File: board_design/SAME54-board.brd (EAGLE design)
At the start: 86.2 x 72.6 mm, 28 parts, among them IC1 ATSAME54N20A-AUT, J2 1985920

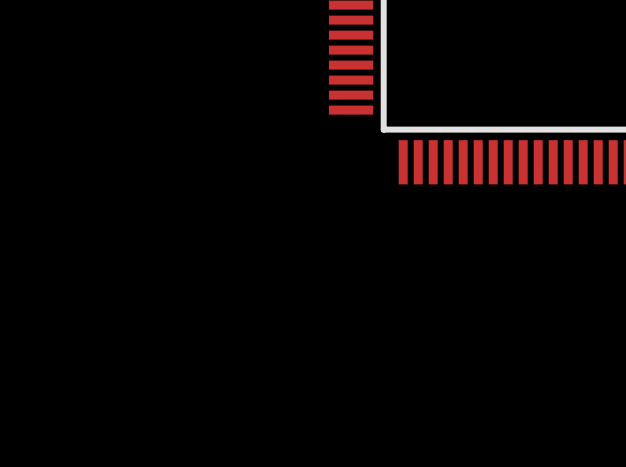
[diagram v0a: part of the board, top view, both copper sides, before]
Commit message: Added power and max20034 to schematic
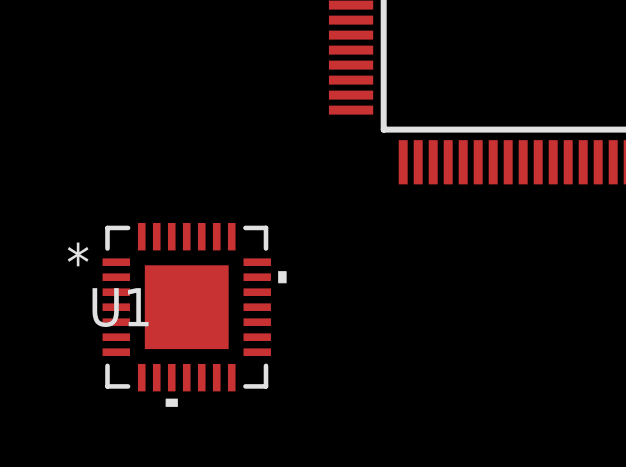
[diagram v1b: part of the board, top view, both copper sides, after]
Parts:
- added U1: MAX20034ATIS/VY+, LAMS_lib:21-100130_MXM
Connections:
- new net AGND: U1.9
- new net EPAD: U1.29
- new net PGND1: U1.3
- new net PGND2: U1.20
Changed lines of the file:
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@@
 <attribute name="VALUE" x="-33.02" y="35.81" size="1.27" layer="27" align="center"/>
+</element>
+<element name="U1" library="LAMS_lib" package="21-100130_MXM" value="MAX20034ATIS/VY+" x="-69.095034375" y="-3.679315625" smashed="yes">
+<attribute name="MANUFACTURER_PART_NUMBER" value="MAX20034ATISVY+" x="-69.095034375" y="-3.679315625" size="1.778" layer="27" display="off"/>
+<attribute name="NAME" x="-72.371634375" y="-4.314315625" size="1.27" layer="25" ratio="6" rot="SR0"/>
+<attribute name="VENDOR" value="Maxim Integrated Products" x="-69.095034375" y="-3.679315625" size="1.778" layer="27" display="off"/>
 </element>
 </elements>
@@
 <contactref element="IC1" pad="26"/>
 </signal>
+<signal name="PGND1">
+<contactref element="U1" pad="3"/>
+</signal>
+<signal name="AGND">
+<contactref element="U1" pad="9"/>
+</signal>
+<signal name="PGND2">
+<contactref element="U1" pad="20"/>
+</signal>
+<signal name="EPAD">
+<contactref element="U1" pad="29"/>
+</signal>
 </signals>

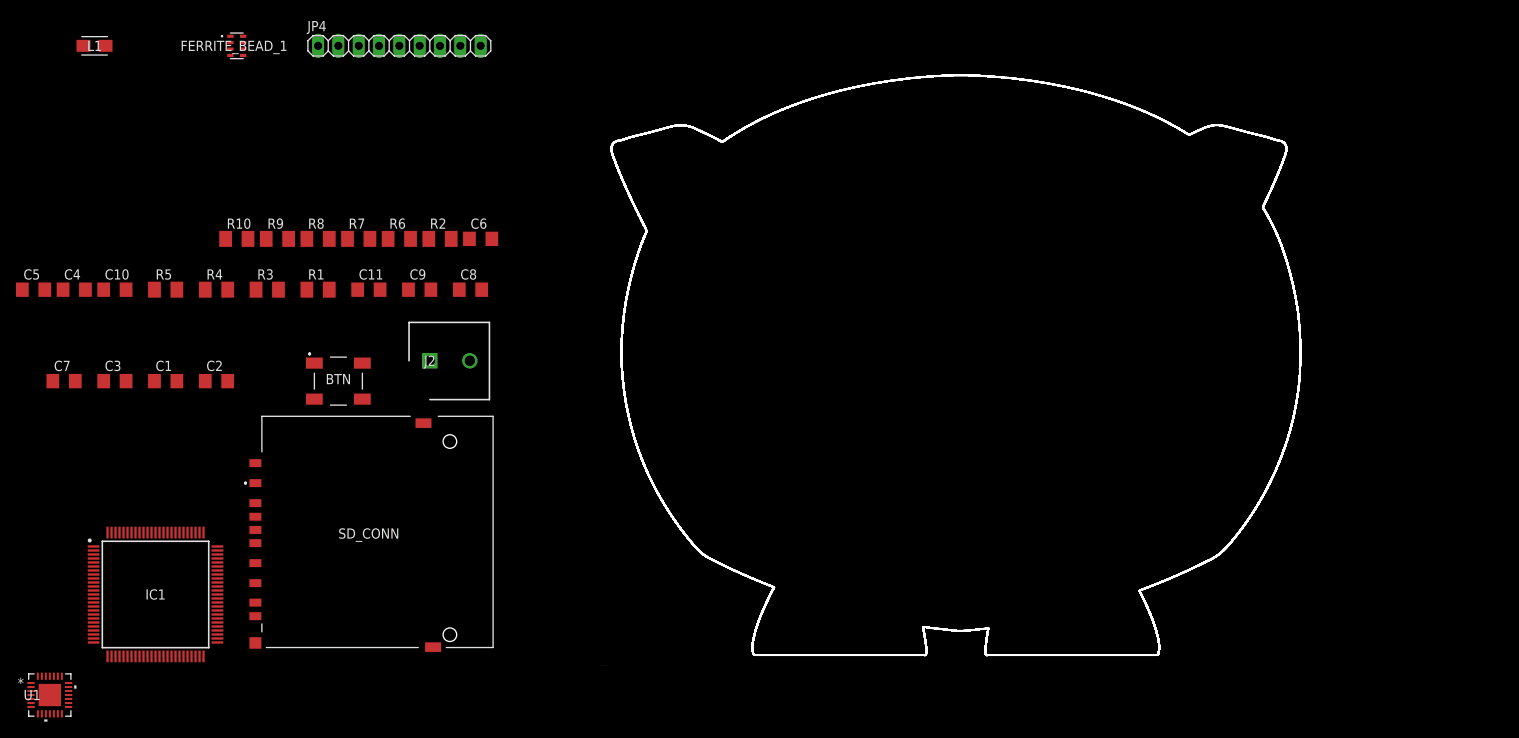
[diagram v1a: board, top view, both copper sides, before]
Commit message: Finished custom SAME54 design. Ready to order
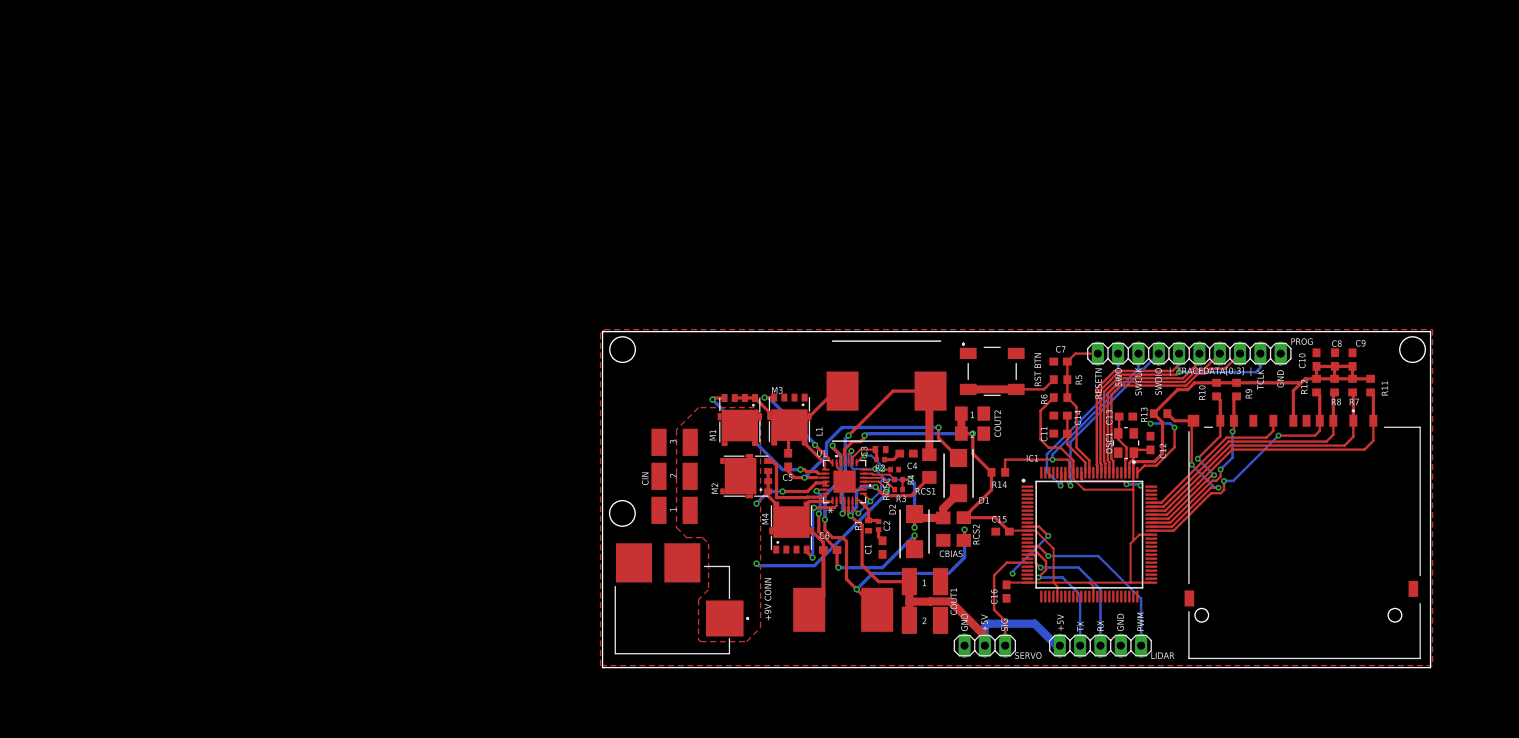
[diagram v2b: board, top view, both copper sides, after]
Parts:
- removed BTN: LL3301BF065QJ, SamacSys_Parts:LL3301BF065QJ
- removed FERRITE_BEAD_1: BLA31AG221SN4D, SamacSys_Parts:BLA31AG102SN4D
- removed J2: 1985920, SamacSys_Parts:SHDR2W110P0X500_1X2_1000X950X1
- removed JP4: (no value), pinhead:1X09
- removed SD_CONN: GSD09002SEU, SamacSys_Parts:GSD09002SEU
- added C12, C13: 8p, rcl:C0603
- added C14: 4.7u, rcl:C0603
- added C15, C16: 100n, rcl:C0603
- added CBIAS: 6.8u, rcl:C1206
- added CIN_1, CIN_2, CIN_3, COUT1_1, COUT1_2: 33u, rcl:C1812
- added COUT2_1, COUT2_2: 22u, rcl:C1206
- added D1, D2: MBRS140T3G, LAMS_lib:DIOM5436X247N
- added J1: PJ-070BH-SMT-TR, LAMS_lib:PJ070BHSMTTR
- added L2: MSS1260-682MLB, LAMS_lib:MSS1260
- added LIDAR: (no value), pinhead:1X05
- added M1, M2, M3, M4: NVMFS5C468NL, LAMS_lib:DFN5_SO-8FL
- added OSC1: CX3225CA12000D0KPSC1CX3225CA, LAMS_lib:OSCCC320X250X90N
- added PROG: (no value), pinhead:1X10
- added R11: 100k, rcl:R0603
- added R12, R13: 10k, rcl:R0603
- added R14: 1k, rcl:R0603
- added RCS1: 8.2m, rcl:R1206
- added RCS2: 20m, rcl:R1206
- added RESET_BTN: LL3301BF065QJ, LAMS_lib:LL3301BF065QJ
- added ROSC: 46.4k, rcl:R0402
- added SD_CARD_CONN: GSD09002SEU, LAMS_lib:GSD09002SEU
- added SERVO: (no value), pinhead:1X03
- C1: value 100n -> 4.7n; device rcl:C1206 -> rcl:C0603
- C10: value 4.7u -> 100n; device rcl:C1206 -> rcl:C0603
- C11, C7, C8: device rcl:C1206 -> rcl:C0603
- C2: value 10uF/10V -> 4.7p; device rcl:C1206 -> rcl:C0402
- C3: value 100n -> 4.7p; device rcl:C1206 -> rcl:C0402
- C4: value 10u -> 4.7n; device rcl:C1206 -> rcl:C0603
- C5, C6: value 10u -> 100n; device rcl:C1206 -> rcl:C0603
- C9: value 100n -> 10u; device rcl:C1206 -> rcl:C0603
- IC1: device SamacSys_Parts:QFP50P1600X1600X120-100N -> LAMS_lib:QFP50P1600X1600X120-100N
- L1: value LQH31MN100J03L -> SRP1238A-3R3M; device SamacSys_Parts:LQH31CN100K03L -> LAMS_lib:INDPM135125X350N
- R1: value 100k -> 10.5k; device rcl:M1206 -> rcl:R0402
- R10: value 1k -> 100k; device rcl:M1206 -> rcl:R0603
- R2: value 10k -> 10.2k; device rcl:M1206 -> rcl:R0402
- R3, R4: value 100k -> 51k; device rcl:M1206 -> rcl:R0402
- R5: value 100k -> 330; device rcl:M1206 -> rcl:R0603
- R6, R8: device rcl:M1206 -> rcl:R0603
- R7: value 10k -> 100k; device rcl:M1206 -> rcl:R0603
- R9: value 330 -> 100k; device rcl:M1206 -> rcl:R0603
- moved C10 150.5 mm to (89.2, 38.2), turned to 90 degrees
- moved R8 128.4 mm to (91.5, 35.0), turned to 90 degrees
- moved R7 125.6 mm to (93.8, 35.0), turned to 90 degrees
- moved C7 124.6 mm to (57.2, 38.0), turned to 180 degrees
- moved R10 123.9 mm to (76.8, 34.5), turned to 90 degrees
- moved R9 121.4 mm to (79.2, 34.5), turned to 90 degrees
- moved IC1 117.0 mm to (60.9, 16.4)
- moved C9 116.9 mm to (93.8, 38.2), turned to 90 degrees
- moved R5 112.4 mm to (57.2, 35.8)
- moved C8 108.4 mm to (91.5, 38.3), turned to 90 degrees
- moved L1 108.0 mm to (35.5, 34.3)
- moved C4 106.0 mm to (38.0, 26.5)
- moved U1 102.9 mm to (30.2, 23.0), turned to 90 degrees
- moved C5 96.7 mm to (23.2, 25.7), turned to 270 degrees
- moved C3 96.1 mm to (34.8, 27.0)
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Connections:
- removed net AGND: U1.9
- removed net EPAD: U1.29
- removed net N$2: R2.1, SD_CONN.2
- removed net PGND1: U1.3
- removed net PGND2: U1.20
- removed net SDDAT[0]: IC1.27, R3.1, SD_CONN.7
- removed net SDDAT[1]: IC1.28, R4.1, SD_CONN.8
- removed net SDDAT[2]: IC1.29, R5.1, SD_CONN.9
- removed net SDDAT[3]: IC1.32, R1.1, SD_CONN.1
- removed net VCC: C1.1, C2.1, J2.1, R1.2, R10.2, R2.2, R3.2, R4.2, R5.2, R6.2, R7.2, R8.2, SD_CONN.4
- removed net VDDANA: C6.1, C8.1, FERRITE_BEAD_1.5, FERRITE_BEAD_1.6, FERRITE_BEAD_1.7, FERRITE_BEAD_1.8, IC1.12
- removed net VDDIO: C5.1, C9.1, FERRITE_BEAD_1.1, FERRITE_BEAD_1.2, FERRITE_BEAD_1.3, FERRITE_BEAD_1.4, IC1.39, IC1.51, IC1.63, IC1.77, IC1.92
- removed net VDDIOB: C4.1, C7.1, IC1.25, IC1.30
- removed net VSW: IC1.91, L1.2
- new net +3V3: C10.1, C15.1, C16.1, C8.1, C9.1, COUT2_1.1, COUT2_2.1, IC1.12, IC1.25, IC1.30, IC1.39, IC1.51, IC1.63, IC1.77, IC1.92, R10.2, R11.2, R12.2, R13.2, R14.2, R6.2, R7.2, R8.2, R9.2, RCS2.2, SD_CARD_CONN.4, U1.18
- new net +5V: COUT1_1.1, COUT1_2.1, LIDAR.1, RCS1.2, SERVO.2, U1.10, U1.5
- new net +9V: CIN_1.1, CIN_2.1, CIN_3.1, J1.1, M1.D1, M1.D2, M1.D3, M1.D4, M2.D1, M2.D2, M2.D3, M2.D4, U1.11, U1.25, U1.26
- new net BIAS: CBIAS.1, D1.2, D2.2, R3.1, R4.1, U1.14, U1.17, U1.6, U1.8
- new net BST1: C6.2, D2.1, U1.27
- new net BST2: C5.2, D1.1, U1.24
- new net COMP1: C2.1, R1.2, U1.7
- new net COMP2: C3.1, R2.2, U1.16
- new net CS1: L1.2, RCS1.1, U1.4
- new net CS2: L2.P$2, RCS2.1, U1.19
- new net DH1: M2.G, U1.28
- new net DH2: M1.G, U1.23
- new net DL1: M4.G, U1.2
- new net DL2: M3.G, U1.21
- new net FOSC: ROSC.2, U1.15
- new net LIDAR_PWM: IC1.16, LIDAR.5
- new net LIDAR_RX: IC1.18, LIDAR.3
- new net LIDAR_TX: IC1.17, LIDAR.2
- new net LX1: C6.1, L2.P$1, M2.S1, M2.S2, M2.S3, M4.D1, M4.D2, M4.D3, M4.D4, U1.1
- new net LX2: C5.1, L1.1, M1.S1, M1.S2, M1.S3, M3.D1, M3.D2, M3.D3, M3.D4, U1.22
- new net N$1: C1.1, R1.1
- new net N$3: C4.1, R2.1
- new net PGOOD1: R3.2, U1.12
- new net PGOOD2: R4.2, U1.13
- new net SDDAT0: IC1.66, R9.1, SD_CARD_CONN.7
- new net SDDAT1: IC1.67, R10.1, SD_CARD_CONN.8
- new net SDDAT2: IC1.68, R11.1, SD_CARD_CONN.9
- new net SDDAT3: IC1.69, R7.1, SD_CARD_CONN.1
- new net SERVO_PWM: IC1.20, SERVO.1
- new net XIN1: C12.1, IC1.78, OSC1.1
- new net XOUT1: C13.1, IC1.79, OSC1.3
- net GND: now also C12.2, C13.2, C14.2, C15.2, C16.2, CBIAS.2, CIN_1.2, CIN_2.2, CIN_3.2, COUT1_1.2, COUT1_2.2, COUT2_1.2, COUT2_2.2, J1.2, J1.3, LIDAR.4, M3.S1, M3.S2, M3.S3, M4.S1, M4.S2, M4.S3, PROG.10, RESET_BTN.1, RESET_BTN.2, ROSC.1, SD_CARD_CONN.3, SD_CARD_CONN.6, SD_CARD_CONN.G1, SD_CARD_CONN.G2, SERVO.3, U1.20, U1.29, U1.3, U1.9; no longer BTN.1, BTN.2, C5.2, C6.2, J2.2, SD_CONN.3, SD_CONN.6, SD_CONN.G1, SD_CONN.G2
- net N$4: now also R5.1, RESET_BTN.3, RESET_BTN.4; no longer BTN.3, BTN.4, R9.2
- net RESETN: now also C7.1, PROG.1, R5.2, R6.1; no longer C3.1, JP4.1, R8.1, R9.1
- net SDCD: now also IC1.64, R12.1, SD_CARD_CONN.CD1; no longer IC1.34, R6.1, SD_CONN.CD1
- net SDCK: now also IC1.71, SD_CARD_CONN.5; no longer IC1.33, SD_CONN.5
- net SDCMD: now also IC1.70, R8.1, SD_CARD_CONN.2; no longer IC1.26
- net SDWP: now also IC1.65, R13.1, SD_CARD_CONN.WP1; no longer IC1.35, R7.1, SD_CONN.WP1
- net SWDCLK: now also PROG.3, R14.1; no longer JP4.3, R10.1
- net SWDIO: now also PROG.4; no longer JP4.4
- net SWO: now also PROG.2; no longer JP4.2
- net TRACECLK: now also PROG.9; no longer JP4.9
- net TRACEDATA[0]: now also PROG.5; no longer JP4.5
- net TRACEDATA[1]: now also PROG.6; no longer JP4.6
- net TRACEDATA[2]: now also PROG.7; no longer JP4.7
- net TRACEDATA[3]: now also PROG.8; no longer JP4.8
- net VDDCORE: now also C14.1; no longer C10.1, L1.1
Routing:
- net +3V3: track 0.00 -> 166.6 mm, vias 0 -> 2
- net +5V: track 0.00 -> 61.6 mm, vias 0 -> 2
- net CS2: track 0.00 -> 47.8 mm, vias 0 -> 4
- net BIAS: track 0.00 -> 40.1 mm, vias 0 -> 6
- net GND: track 0.00 -> 37.9 mm, vias 0 -> 6
- net SDDAT2: track 0.00 -> 37.8 mm
- net +9V: track 0.00 -> 37.7 mm, vias 0 -> 4
- net SDDAT3: track 0.00 -> 34.7 mm
- net TRACECLK: track 0.00 -> 33.3 mm, vias 0 -> 1
- net CS1: track 0.00 -> 32.4 mm, vias 0 -> 2
- net SDCD: track 0.00 -> 31.9 mm, vias 0 -> 2
- net SDCMD: track 0.00 -> 31.8 mm
- net BST2: track 0.00 -> 30.7 mm, vias 0 -> 2
- net LX1: track 0.00 -> 30.2 mm
- net LX2: track 0.00 -> 29.6 mm
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- added copper zone on layer 1, net +9V
- added copper zone on layer 1, net GND
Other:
- board size 86.2 x 72.6 mm -> 103.5 x 42 mm
- board text added: "+5V"
- board text added: "+9V CONN"
- board text added: "1"
- board text added: "2"
- board text added: "3"
- board text added: "CIN"
- board text added: "COUT1"
- board text added: "COUT2"
- board text added: "D1"
- board text added: "GND"
- board text added: "IC1"
- board text added: "L1"
- board text added: "LIDAR"
- board text added: "PROG"
- board text added: "PWM"
- board text added: "R3"
- board text added: "RESETN"
- board text added: "RST BTN"
- board text added: "RX"
- board text added: "SERVO"
- board text added: "SIG"
- board text added: "SWCLK"
- board text added: "SWDIO"
- board text added: "SWO"
- board text added: "TCLK"
- board text added: "TX"
- board text added: "| TRACEDATA[0:3] |"
- board text removed: "C:/Users/Kris/Desktop/LAMS/lams-logo_PCB-OUTLINE.bmp"

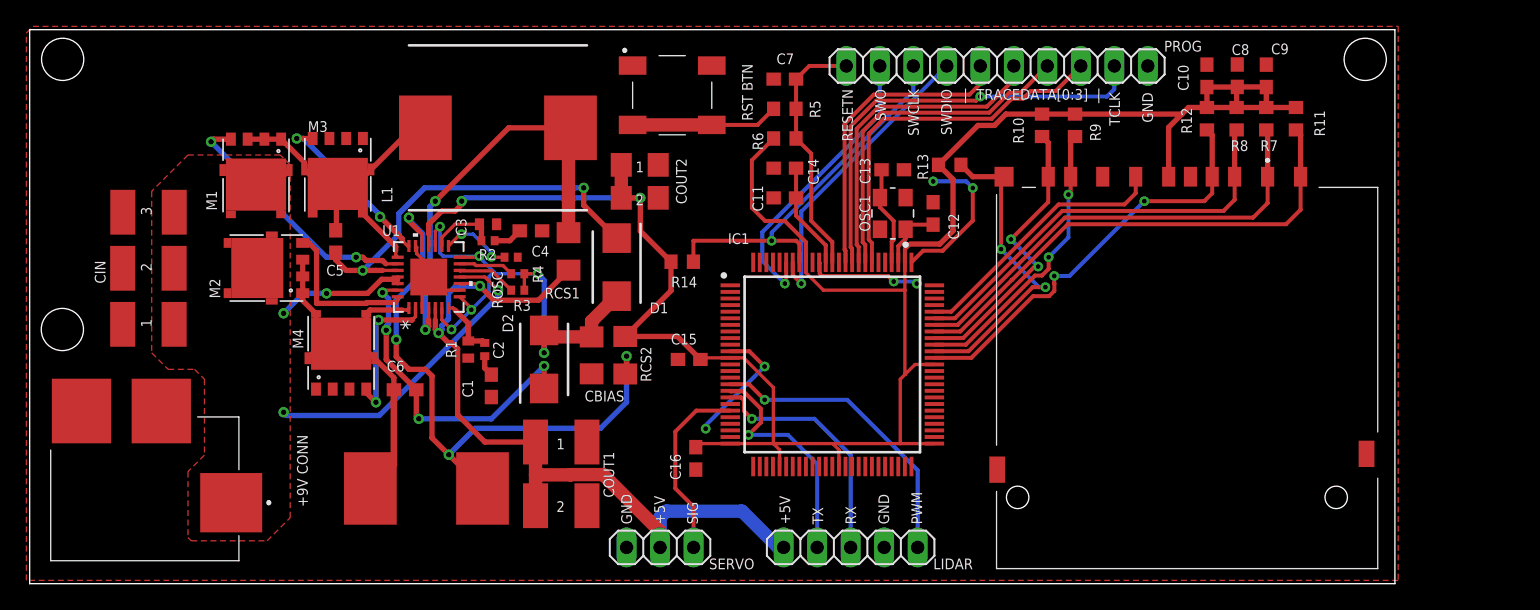
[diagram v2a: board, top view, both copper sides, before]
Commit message: Added diskio and fatfs middleware for file writing
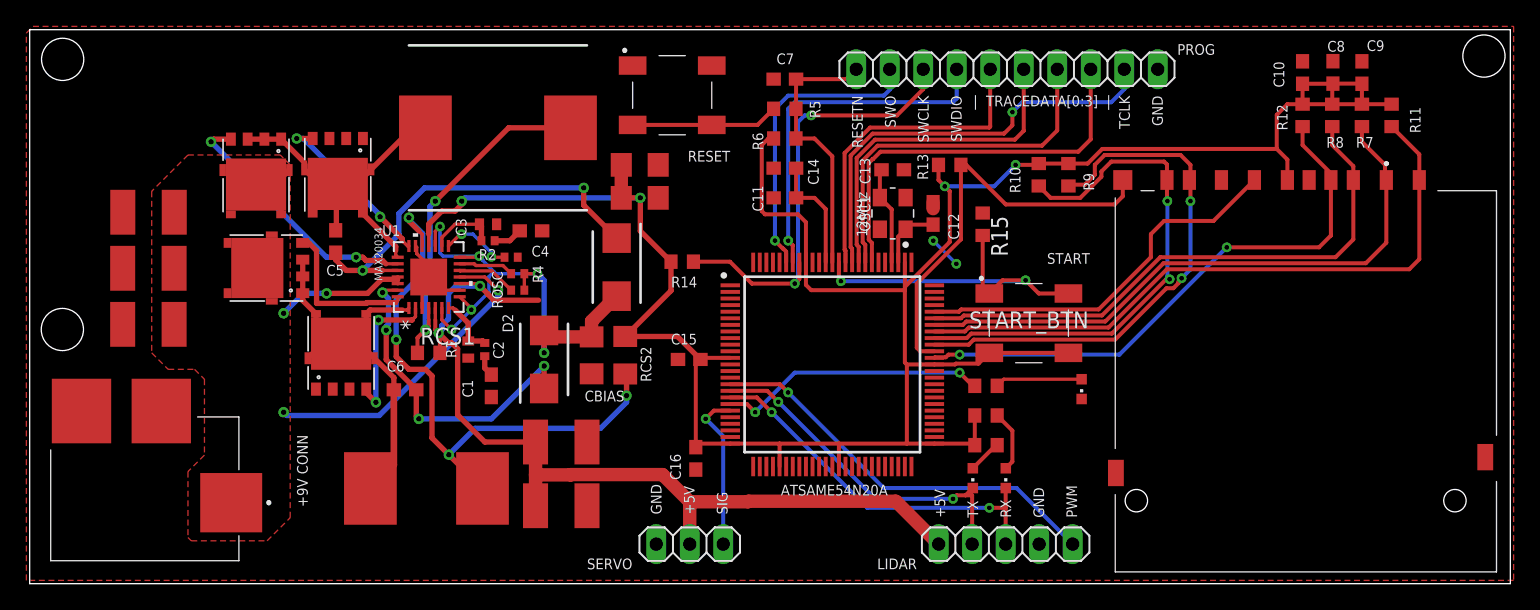
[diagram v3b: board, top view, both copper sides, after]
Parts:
- added LED_RX, LED_STATUS, LED_TX: (no value), led:CHIPLED_0603
- added R15: 10k, rcl:R0603
- added R16, R17, R18: (no value), rcl:R0603
- added START_BTN: LL3301BF065QJ, LAMS_lib:LL3301BF065QJ
- RCS1: value 8.2m -> 10m; device rcl:R1206 -> rcl:R0603
- moved RCS1 13.1 mm to (30.2, 17.2), turned to 0 degrees
- moved LIDAR 11.8 mm to (74.0, 2.75)
- moved SD_CARD_CONN 9.00 mm to (96.5, 16.2)
- moved C10 7.25 mm to (96.5, 38.5)
- moved C8 7.25 mm to (98.8, 38.5)
- moved C9 7.25 mm to (101.0, 38.5)
- moved R11 7.25 mm to (103.2, 35.2)
- moved R12 7.25 mm to (96.5, 35.2)
- moved R7 7.25 mm to (101.0, 35.2)
- moved R8 7.25 mm to (98.8, 35.2)
- moved R9 3.78 mm to (78.8, 30.8)
- moved R10 3.76 mm to (76.5, 30.8)
- moved SERVO 2.26 mm to (50.0, 2.75)
- moved PROG 0.79 mm to (74.1, 38.8)
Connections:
- new net LED_STATUS: IC1.19, R16.2
- new net N$2: LED_STATUS.A, R16.1
- new net N$8: LED_RX.A, R17.1
- new net N$9: LED_TX.A, R18.1
- new net START_BTN: IC1.87, R15.2, START_BTN.1, START_BTN.2
- net +3V3: now also R17.2, R18.2, START_BTN.3, START_BTN.4
- net GND: now also LED_STATUS.C, R15.1
- net LIDAR_RX: now also LED_RX.C
- net LIDAR_TX: now also LED_TX.C
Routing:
- net START_BTN: track 0.00 -> 27.0 mm, vias 0 -> 2
- net GND: track 37.9 -> 11.0 mm, vias 6 -> 2
- net +3V3: track 166.6 -> 187.6 mm, vias 2 -> 4
- net LED_STATUS: track 0.00 -> 20.5 mm, vias 0 -> 2
- net SDDAT0: track 21.9 -> 40.9 mm
- net SDDAT1: track 22.2 -> 40.0 mm
- net SDDAT2: track 37.8 -> 50.0 mm
- net SDDAT3: track 34.7 -> 46.4 mm
- net SDCMD: track 31.8 -> 43.5 mm
- net SDCD: track 31.9 -> 43.0 mm
- net LIDAR_RX: track 18.4 -> 28.8 mm, vias 1 -> 2
- net SDCK: track 20.2 -> 29.4 mm
- net +5V: track 61.6 -> 70.5 mm
- net LIDAR_TX: track 17.7 -> 26.3 mm, vias 1 -> 2
- net LIDAR_PWM: track 22.8 -> 31.0 mm
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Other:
- board size 103.5 x 42 mm -> 112.2 x 42 mm
- board text added: "12MHz"
- board text added: "ATSAME54N20A"
- board text added: "MAX20034"
- board text added: "RESET"
- board text added: "START"
- board text removed: "1"
- board text removed: "2"
- board text removed: "3"
- board text removed: "CIN"
- board text removed: "COUT1"
- board text removed: "COUT2"
- board text removed: "D1"
- board text removed: "IC1"
- board text removed: "L1"
- board text removed: "R3"
- board text removed: "RST BTN"
